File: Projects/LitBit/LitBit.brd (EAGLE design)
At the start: 160 x 100 mm, 73 parts, among them U1 24FC1025, U2 MCP7490N, U3 ADXL345, U5 S-1335J33-M5T1U3, U6 nRF8001, U7 MCP73831, U8 ATMEGA32U4-MUR-QFN44, Y1 16.0000 MHz, Y2 32.7680 kHz, Y3 32.7680 kHz, Y4 8.0000 MHz

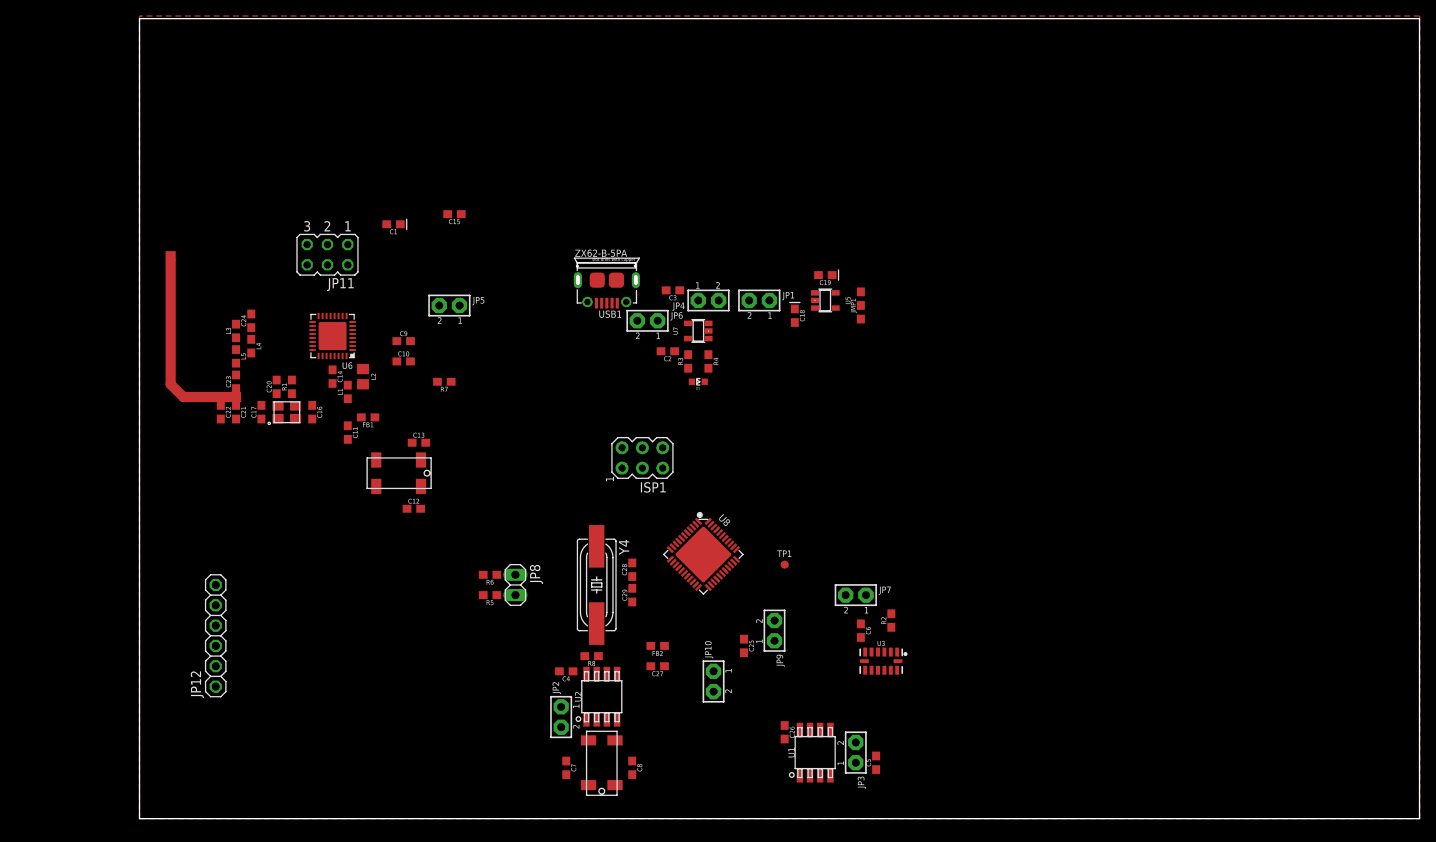
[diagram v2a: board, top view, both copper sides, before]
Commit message: Start Layout, change uP package, add display, add JTAG, add battery connector.
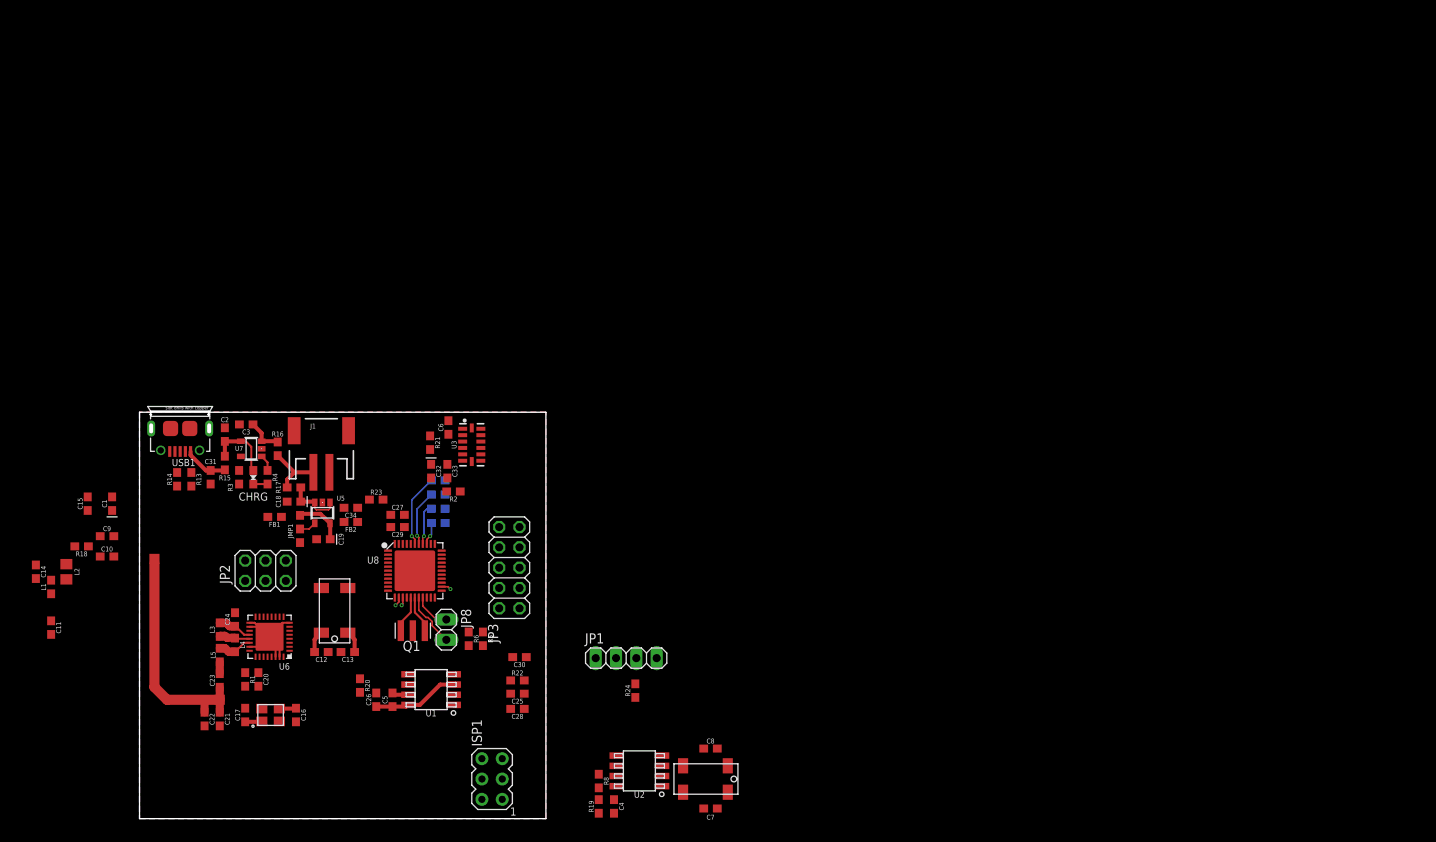
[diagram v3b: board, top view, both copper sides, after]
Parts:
- removed D1: Green, Wurth_Elektronik_Optoelectronics_rev18a:WL-SMCW_0603
- removed JP10, JP4, JP5, JP6, JP7, JP9: (no value), microbuilder:JUMPER2
- removed JP11: BLE_SPI, jumper:JP3Q
- removed JP12: Display, adafruit:1X06
- removed R7: 0R, SCADA_CUSTOM_LIBRARY:0603-CUSTOM
- removed TP1: TEST_POINT_40MIL_DIA, SCADA_CUSTOM_LIBRARY:TEST_POINT_40MIL_DIA
- removed Y4: 8.0000 MHz, adafruit:HC49UP
- added C30, C31, C34: 1uF, SCADA_CUSTOM_LIBRARY:0603-CUSTOM
- added C32: 10uF, SCADA_CUSTOM_LIBRARY:0603-POLAR
- added C33: 100n, SCADA_CUSTOM_LIBRARY:0603-CUSTOM
- added CHRG: Green, SCADA_CUSTOM_LIBRARY:0603-LED
- added J1: Battery, SparkFun-Connectors:JST-2-SMD
- added Q1: CSTCR6M00G53Z, murata-filter:CSTCR6M
- added R10, R11, R12, R13, R14, R9: 10k, SCADA_CUSTOM_LIBRARY:0603-CUSTOM
- added R15, R16, R17, R18, R19, R20, R21, R22, R23, R24: 0, SCADA_CUSTOM_LIBRARY:0603-CUSTOM
- C26: value 1uF -> 4.7 uF
- C28: value 22p -> 100n
- C29: value 22p -> 4.7uF
- JP1: value (none) -> Display; device microbuilder:JUMPER2 -> pinhead:1X04
- JP2: device microbuilder:JUMPER2 -> pinhead:2X03
- JP3: value (none) -> JTAG; device microbuilder:JUMPER2 -> pinhead:2X05
- R5, R6: value 10k -> 2.2k
- moved JMP1 75.5 mm to (20.1, 36.2)
- moved C19 70.9 mm to (23.0, 34.9)
- moved U5 68.2 mm to (22.9, 38.2), turned to 180 degrees
- moved C18 66.8 mm to (19.3, 39.6), turned to 180 degrees
- moved C5 61.0 mm to (31.6, 14.9)
- moved C15 58.4 mm to (-6.48, 39.4), turned to 90 degrees
- moved R3 58.0 mm to (12.4, 42.7)
- moved U3 57.9 mm to (41.5, 46.7), turned to 90 degrees
- moved U7 57.8 mm to (14.0, 46.2)
- moved C6 57.5 mm to (38.6, 48.9), turned to 90 degrees
- moved R2 57.1 mm to (39.2, 40.9), turned to 180 degrees
- moved R4 57.0 mm to (16.0, 42.7)
- moved USB1 56.5 mm to (5.08, 48.8)
- moved C2 56.3 mm to (10.7, 48.0), turned to 90 degrees
- moved C3 55.9 mm to (13.3, 49.3)
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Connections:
- removed net N$28: C25.1, JP9.1, U8.14, U8.34
- removed net N$32: FB2.2, JP10.1
- removed net N$33: C27.1, FB2.1, U8.24, U8.44
- removed net N$34: TP1.TP$1
- removed net N$9: C6.2, JP7.1, U3.6
- removed net SHIELD: USB1.5, USB1.P1, USB1.P2, USB1.P3, USB1.P4, USB1.P5, USB1.P6
- new net ADXL_INT1: U3.8, U8.21
- new net ADXL_INT2: U3.9, U8.25
- new net CHRG_IN: C2.1, CHRG.2, R15.2, U7.4
- new net N$36: C32.1, C33.1, C6.2, R21.2, U3.1, U3.6
- new net TCK: JP3.1, R10.1, U8.39
- new net TDI: JP3.9, R11.1, U8.36
- new net TDO: JP3.3, R12.1, U8.37
- new net TMS: JP3.5, R9.1, U8.38
- new net UP_AVCC: C27.1, C29.2, R23.2, U8.24, U8.44
- new net UP_D+: R14.1, U8.4
- new net UP_D-: R13.1, U8.3
- new net UP_PWR: C25.1, C28.1, C30.2, JP3.4, R10.2, R11.2, R12.2, R22.2, R9.2, U8.14, U8.34, U8.6
- new net UVCC: U8.2
- net 3.3V: now also FB2.2, R18.1, R19.1, R20.1, R22.1, R24.1, U3.7; no longer JP2.2, JP3.2, JP5.2, JP9.2, R7.1
- net ACTIVE: now also U8.12
- net AGND: now also C27.2, C29.1, C32.2, C33.2, C34.2, C6.1, R2.2, U8.42; no longer R2.1
- net AVCC: now also C34.1, FB2.1, R21.1, R23.1; no longer JP10.2, JP7.2, R7.2
- net D+: now also R14.2; no longer U8.4
- net D-: now also R13.2; no longer U8.3
- net GND: now also C28.2, C30.1, C31.2, J1.2, JP1.4, JP3.10, JP3.2, Q1.2, R2.1, U3.12, USB1.5, USB1.P1, USB1.P2, USB1.P3, USB1.P4, USB1.P5, USB1.P6; no longer C27.2, C28.1, C29.1, C6.1, R2.2
- net MISO: now also JP2.2, U8.11; no longer JP11.5
- net MISO_3V3: now also JP2.1; no longer JP11.6
- net MOSI: now also JP2.4, U8.10; no longer JP11.3
- net MOSI_3V3: now also JP2.3; no longer JP11.4
- net N$14: now also R17.2; no longer JP1.1
- net N$15: now also R19.2; no longer JP2.1
- net N$16: now also R16.2; no longer JP4.1
- net N$17: now also R20.2; no longer JP3.1
- net N$25: now also CHRG.1; no longer D1.1
- net N$29: now also Q1.1, U8.17; no longer C28.2, U8.16, Y4.1
- net N$30: now also Q1.3, U8.16; no longer C29.2, U8.17, Y4.2
- net N$7: now also JP1.3, R24.2; no longer C2.1, D1.2, JP6.1, U7.4
- net N$8: now also R18.2; no longer JP5.1
- net RDYN: now also U8.20
- net RST: now also JP3.6
- net RST_NRF: now also U8.8
- net SCK: now also JP2.6, U8.9; no longer JP11.1
- net SCK_3V3: now also JP2.5; no longer JP11.2
- net SCL: now also JP1.1, U8.18
- net SDA: now also JP1.2, U8.19
- net V_BATT: now also J1.1, R16.1, R17.1; no longer JP1.2, JP4.2
- net V_USB: now also C31.1, R15.1; no longer JP6.2
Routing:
- net GND: track 0.00 -> 17.2 mm
- net N$17: track 0.00 -> 10.9 mm
- net TCK: track 0.00 -> 9.13 mm, vias 0 -> 1
- net CHRG_IN: track 0.00 -> 8.52 mm
- net V_BATT: track 0.00 -> 8.32 mm
- net N$14: track 0.00 -> 7.13 mm
- net TMS: track 0.00 -> 7.01 mm, vias 0 -> 1
- net SCL: track 0.00 -> 6.86 mm
- net N$24: track 0.00 -> 6.52 mm
- net 3.3V: track 0.00 -> 6.32 mm
- net V_USB: track 0.00 -> 5.57 mm
- net TDO: track 0.00 -> 5.16 mm, vias 0 -> 1
- net SDA: track 0.00 -> 4.71 mm
- net N$30: track 0.00 -> 4.66 mm
- net N$29: track 0.00 -> 4.66 mm
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- added copper zone on layer 16, net GND
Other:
- board size 160 x 100 mm -> 50.8 x 50.8 mm

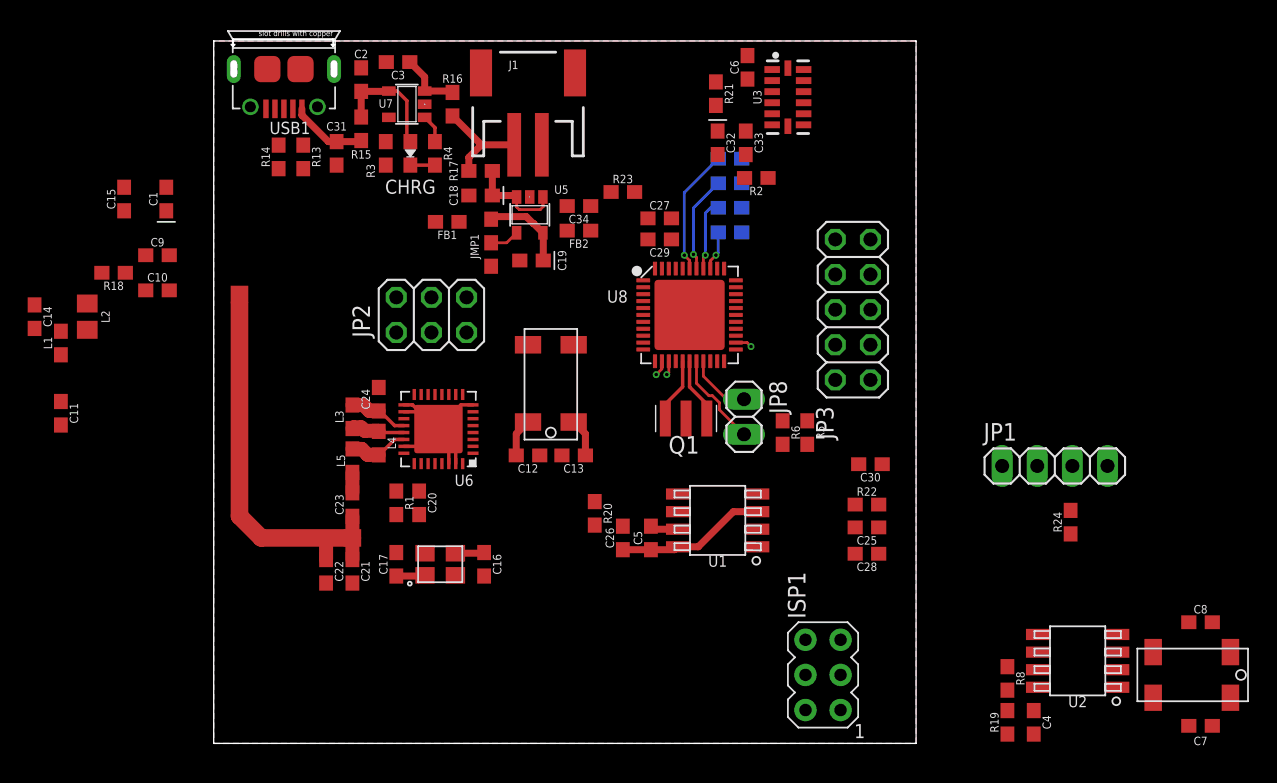
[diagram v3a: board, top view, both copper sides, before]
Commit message: routing, change RTC package
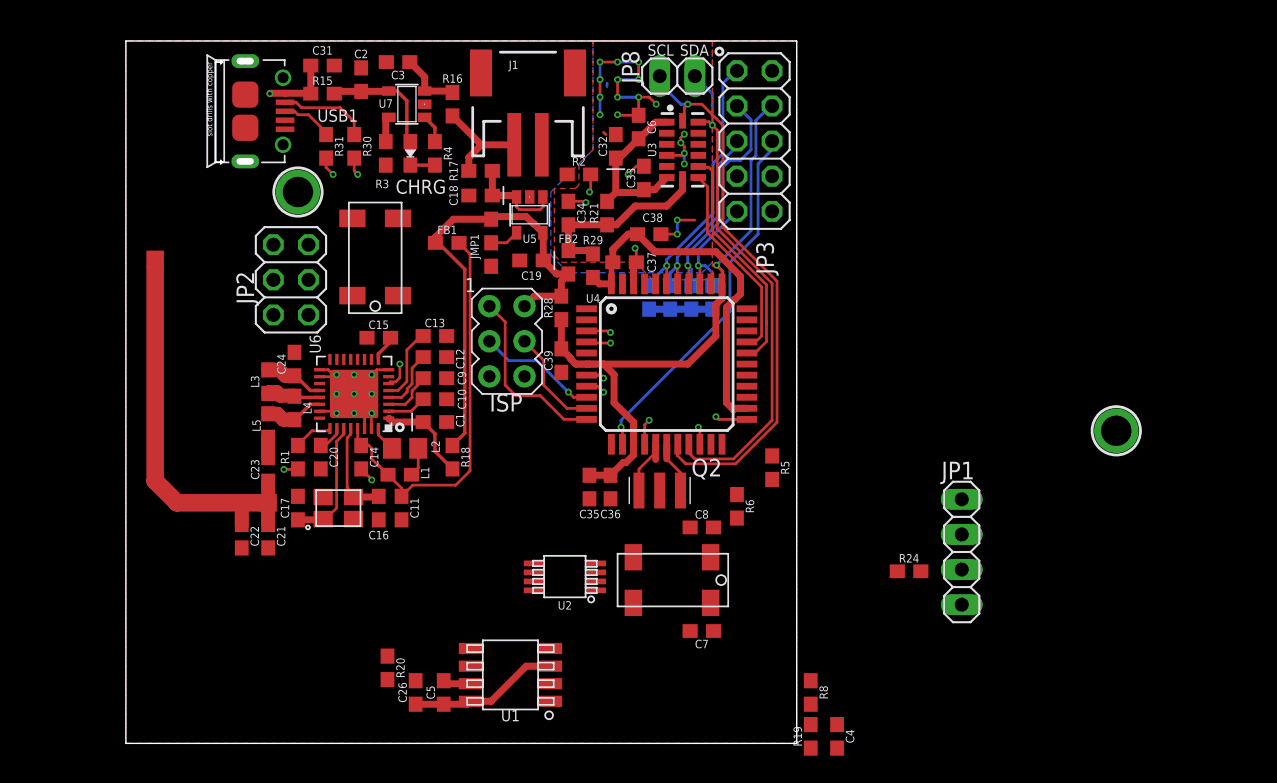
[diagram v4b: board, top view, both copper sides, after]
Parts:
- removed C25, C29: 4.7uF, SCADA_CUSTOM_LIBRARY:0603-CUSTOM
- removed C27, C28: 100n, SCADA_CUSTOM_LIBRARY:0603-CUSTOM
- removed C30: 1uF, SCADA_CUSTOM_LIBRARY:0603-CUSTOM
- removed ISP1: AVRISP-6, adafruit:AVRISP
- removed Q1: CSTCR6M00G53Z, murata-filter:CSTCR6M
- removed R10, R11, R12, R13, R14, R9: 10k, SCADA_CUSTOM_LIBRARY:0603-CUSTOM
- removed R22, R23: 0, SCADA_CUSTOM_LIBRARY:0603-CUSTOM
- removed U8: ATMEGA32U4-MUR-QFN44, Seeed-IC:QFN44G-0.5-7X7MM
- added C35, C38: 4.7uF, SCADA_CUSTOM_LIBRARY:0603-CUSTOM
- added C36, C37: 100n, SCADA_CUSTOM_LIBRARY:0603-CUSTOM
- added C39: 1uF, SCADA_CUSTOM_LIBRARY:0603-CUSTOM
- added GND, U$13: MOUNTINGHOLE2.0, microbuilder:MOUNTINGHOLE_2.0_PLATED
- added ISP: AVRISP-6, adafruit:AVRISP
- added Q2: CSTCR6M00G53Z, murata-filter:CSTCR6M
- added R25, R26, R27, R7: 10k, SCADA_CUSTOM_LIBRARY:0603-CUSTOM
- added R28, R29: 0, SCADA_CUSTOM_LIBRARY:0603-CUSTOM
- added R30, R31: 22, SCADA_CUSTOM_LIBRARY:0603-CUSTOM
- added U4: UP_ATMEGA32U4-AU, SCADA_CUSTOM_LIBRARY:TQFP44
- U2: value MCP7490N -> RTC_MCP7940N8-MSOP; device SCADA_CUSTOM_LIBRARY:8-SOIC_HAND_SOLDER -> SCADA_CUSTOM_LIBRARY:8-MSOP-CUSTOM
- moved Y3 38.2 mm to (33.1, 11.8)
- moved U2 37.6 mm to (25.4, 12.1)
- moved C7 36.7 mm to (35.3, 8.13)
- moved C8 36.7 mm to (35.3, 15.6)
- moved R18 27.9 mm to (17.3, 20.7), turned to 270 degrees
- moved L1 26.3 mm to (13.5, 19.4), turned to 180 degrees
- moved C14 25.7 mm to (10.7, 20.7)
- moved C11 25.6 mm to (13.6, 17.0)
- moved C1 25.3 mm to (16.0, 23.2), turned to 0 degrees
- moved JP8 25.1 mm to (33.5, 48.3), turned to 180 degrees
- moved L2 24.9 mm to (13.8, 21.3), turned to 0 degrees
- moved C9 21.9 mm to (16.0, 26.4)
- moved C10 21.6 mm to (16.0, 24.9)
- moved C15 21.0 mm to (11.9, 29.3), turned to 180 degrees
- moved C26 18.7 mm to (14.6, 3.68)
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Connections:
- removed net N$29: Q1.1, U8.17
- removed net N$30: Q1.3, U8.16
- removed net UP_D+: R14.1, U8.4
- removed net UP_D-: R13.1, U8.3
- removed net UVCC: U8.2
- new net N$28: R31.1, USB1.3
- new net N$31: Q2.1, U4.16
- new net N$32: Q2.3, U4.17
- new net N$9: R30.1, USB1.2
- net 3.3V: now also ISP.2, R28.1; no longer ISP1.2, R22.1, U3.7
- net ACTIVE: now also U4.12; no longer U8.12
- net ADXL_INT1: now also U4.30; no longer U8.21
- net ADXL_INT2: now also U4.29; no longer U8.25
- net AGND: now also C37.2, C38.1, U3.12, U4.42; no longer C27.2, C29.1, U8.42
- net AVCC: now also R29.2, U3.7; no longer R23.1
- net D+: now also R31.2, U4.4; no longer R14.2, USB1.3
- net D-: now also R30.2, U4.3; no longer R13.2, USB1.2
- net GND: now also C35.2, C36.2, C39.1, ISP.6, Q2.2, U2.VBAT, U2.VSS, U4.15, U4.23, U4.35, U4.43, U4.5; no longer C25.2, C28.2, C30.1, ISP1.6, Q1.2, U2.3, U2.4, U3.12, U8.15, U8.23, U8.35, U8.43, U8.5, U8.TAB
- net MFP: now also U2.MFP, U4.21; no longer U2.7
- net MISO: now also ISP.1, U4.11; no longer ISP1.1, U8.11
- net MOSI: now also ISP.4, U4.10; no longer ISP1.4, U8.10
- net N$1: now also U2.X1; no longer U2.1
- net N$15: now also U2.VCC; no longer U2.8
- net N$2: now also U2.X2; no longer U2.2
- net RDYN: now also U4.20; no longer U8.20
- net RST: now also ISP.5, U4.13; no longer ISP1.5, U8.13
- net RST_NRF: now also U4.8; no longer U8.8
- net SCK: now also ISP.3, U4.9; no longer ISP1.3, U8.9
- net SCL: now also U2.SCL, U4.18; no longer U2.6, U8.18
- net SDA: now also U2.SDA, U4.19; no longer U2.5, U8.19
- net TCK: now also R25.1, U4.39; no longer R10.1, U8.39
- net TDI: now also R26.1, U4.36; no longer R11.1, U8.36
- net TDO: now also R27.1, U4.37; no longer R12.1, U8.37
- net TMS: now also R7.1, U4.38; no longer R9.1, U8.38
- net UP_AVCC: now also C37.1, C38.2, R29.1, U4.24, U4.44; no longer C27.1, C29.2, R23.2, U8.24, U8.44
- net UP_PWR: now also C35.1, C36.1, C39.2, R25.2, R26.2, R27.2, R28.2, R7.2, U4.14, U4.34, U4.6; no longer C25.1, C28.1, C30.2, R10.2, R11.2, R12.2, R22.2, R9.2, U8.14, U8.34, U8.6
- net V_USB: now also U4.7; no longer U8.7
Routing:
- net UP_PWR: track 1.03 -> 53.6 mm
- net SCL: track 6.86 -> 41.2 mm, vias 0 -> 1
- net SDA: track 4.71 -> 36.7 mm, vias 0 -> 1
- net AGND: track 0.00 -> 31.1 mm, vias 0 -> 22
- net VDDA: track 0.00 -> 31.0 mm
- net 3.3V: track 6.32 -> 34.3 mm
- net UP_AVCC: track 1.21 -> 26.6 mm, vias 1 -> 0
- net RST: track 1.14 -> 26.5 mm
- net ADXL_INT2: track 0.00 -> 16.9 mm
- net ADXL_INT1: track 0.00 -> 14.7 mm
- net AVCC: track 0.00 -> 14.3 mm
- net MISO: track 0.00 -> 13.2 mm
- net N$36: track 0.00 -> 12.3 mm
- net TDO: track 5.16 -> 17.2 mm
- net GND: track 17.2 -> 28.1 mm, vias 0 -> 13
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- added copper zone on layer 1, net AGND
- added copper zone on layer 16, net AGND
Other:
- board size 50.8 x 50.8 mm -> 48.5 x 50.8 mm
- board text added: "SCL"
- board text added: "SDA"

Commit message: nearly complete layout
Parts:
- removed R28: 0, SCADA_CUSTOM_LIBRARY:0603-CUSTOM
- added U$8: MOUNTINGHOLE2.0, microbuilder:MOUNTINGHOLE_2.0_PLATED
- Y2, Y3: device SCADA_CUSTOM_LIBRARY:4-SOJ -> SCADA_CUSTOM_LIBRARY:2-SMD
- moved JP1 31.4 mm to (24.5, 3.30), turned to 0 degrees
- moved C4 27.6 mm to (18.8, 9.02), turned to 180 degrees
- moved GND 26.6 mm to (45.7, 4.57)
- moved C8 24.9 mm to (13.2, 4.19), turned to 180 degrees
- moved Y3 21.3 mm to (12.3, 7.24), turned to 90 degrees
- moved R24 20.6 mm to (30.7, 5.84), turned to 270 degrees
- moved R20 20.5 mm to (32.9, 8.51), turned to 180 degrees
- moved C7 20.1 mm to (15.2, 9.14), turned to 180 degrees
- moved R31 17.6 mm to (17.8, 28.4), flipped to the bottom
- moved R30 17.5 mm to (19.6, 28.4), flipped to the bottom
- moved FB1 15.7 mm to (25.0, 22.7), turned to 270 degrees
- moved R27 14.3 mm to (41.1, 19.6)
- moved C18 14.3 mm to (25.9, 26.9)
- moved C37 14.3 mm to (36.3, 22.1)
- moved FB2 14.3 mm to (32.3, 22.1)
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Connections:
- removed net N$15: C4.1, R19.2, R8.2, U2.VCC
- removed net UP_PWR: C35.1, C36.1, C39.2, JP3.4, R25.2, R26.2, R27.2, R28.2, R7.2, U4.14, U4.34, U4.6
- new net N$29: C4.1, R19.2, U2.VCC
- net 3.3V: now also C35.1, C36.1, C39.2, JP3.4, R25.2, R26.2, R27.2, R7.2, R8.2, U4.14, U4.34, U4.6; no longer R28.1
- net N$1: now also Y3.P$2; no longer Y3.P4
- net N$2: now also Y3.P$1; no longer Y3.P1
- net N$5: now also Y2.P$1; no longer Y2.P4
- net N$6: now also Y2.P$2; no longer Y2.P1
- net REQN_3V3: now also U4.1
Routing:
- net UP_PWR: track 53.6 -> 0.00 mm, vias 1 -> 0
- net 3.3V: track 34.3 -> 85.0 mm, vias 0 -> 3
- net GND: track 28.1 -> 74.3 mm, vias 13 -> 34
- net RDYN: track 1.28 -> 43.7 mm, vias 1 -> 2
- net V_USB: track 6.38 -> 48.1 mm
- net SCL: track 41.2 -> 79.7 mm, vias 1 -> 5
- net SDA: track 36.7 -> 74.9 mm, vias 1 -> 5
- net RST_NRF: track 1.41 -> 34.9 mm, vias 1 -> 2
- net MFP: track 0.00 -> 30.3 mm, vias 0 -> 2
- net SCK: track 8.70 -> 36.6 mm
- net MOSI: track 7.54 -> 31.5 mm
- net REQN_3V3: track 0.00 -> 23.4 mm, vias 0 -> 2
- net MISO: track 13.2 -> 35.2 mm
- net D+: track 3.16 -> 24.5 mm, vias 2 -> 1
- net ACTIVE: track 1.97 -> 23.2 mm, vias 1 -> 2
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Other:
- board size 48.5 x 50.8 mm -> 48.8 x 38.1 mm
